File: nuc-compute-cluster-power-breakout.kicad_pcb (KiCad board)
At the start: 4 copper layers, 100 x 100 mm, 159 parts, among them J1 USB3106-30-0230-A, J10 10107844-002LF, J2 BM04B-SRSS-TB-LF-SN, J3 BM04B-SRSS-TB-LF-SN, J4 43045-1013, J5 430450812, J6 430450812, J7 430450812, J8 430450812, J9 430450812, Q1 SQS401EN-T1_BE3, Q10 SSM3K15ACT, Q11 BC856,215, Q15 DMN4010LFG-7, Q2 SQS401EN-T1_BE3, Q3 SSM3K15ACT, Q4 SSM3K15ACT, Q5 SQS401EN-T1_BE3, Q6 SSM3K15ACT, Q7 SQS401EN-T1_BE3, Q8 SQS401EN-T1_BE3, Q9 SSM3K15ACT, U1 FT2232HL-REEL, U10 TCA9534, U11 TMCS1100A2-Q1, U12 TMCS1100A2-Q1, U13 TMCS1100A2-Q1, U14 ADS7828, U15 AP62301WU-7, U7 AP62301WU-7, U8 TMCS1100A2-Q1, U9 TMCS1100A2-Q1, Y1 KX-7_12,MHz

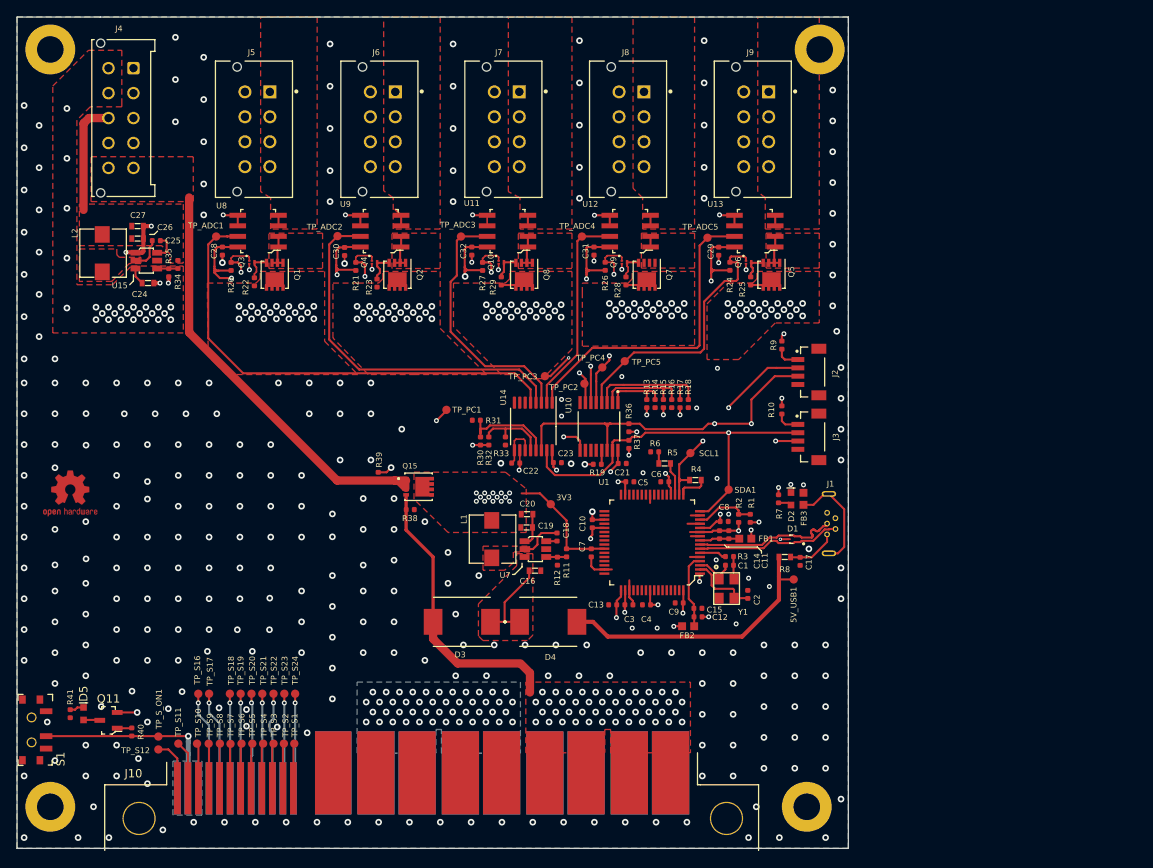
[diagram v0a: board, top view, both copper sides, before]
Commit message: Added board cut-out. Logos replacement
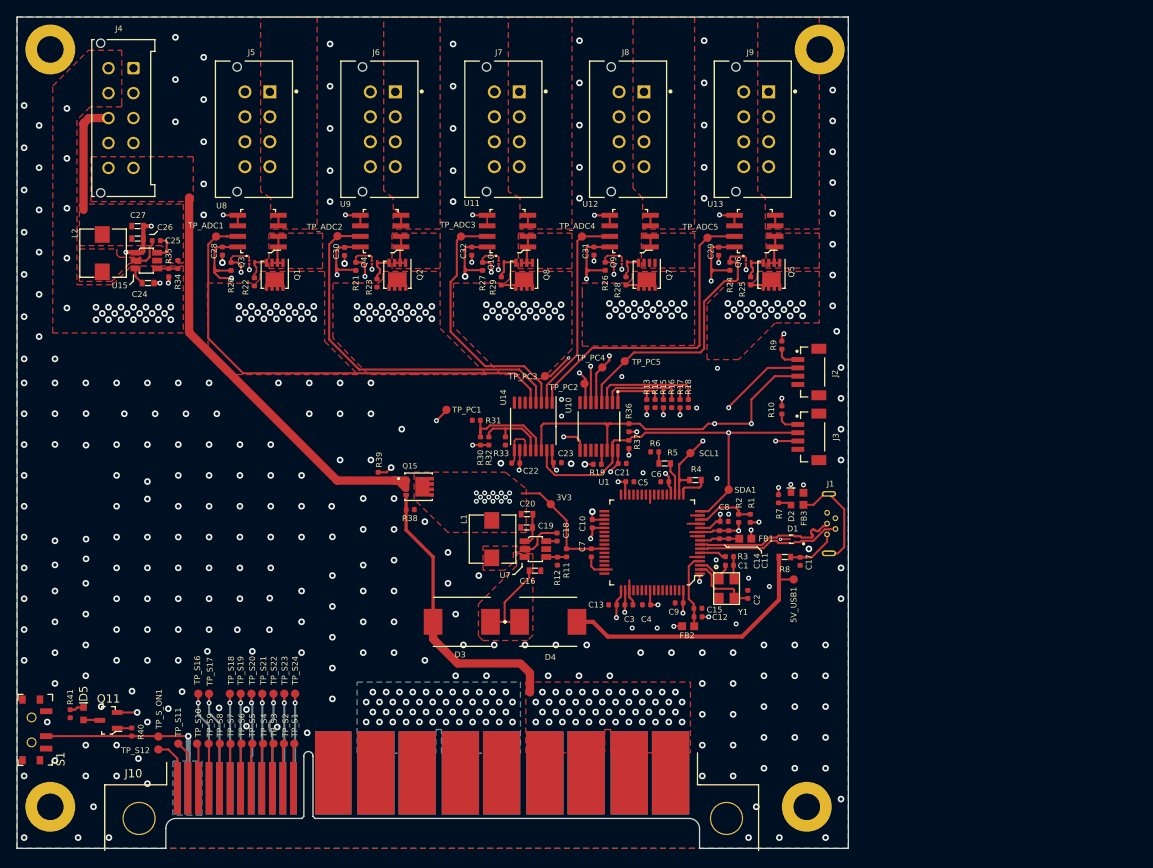
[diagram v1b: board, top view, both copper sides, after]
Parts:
- removed G***: antmicro-logo_scaled_20mm, antmicro-footprints:antmicro-logo_scaled_20mm_mask
- removed REF**: OSHW-Logo2_7.3x6mm_Copper_Mask, antmicro-footprints:OSHW-Logo2_7.3x6mm_Copper_Mask
- added N1: OSHW-Logo_7.5x8mm_Mask, antmicro-footprints:OSHW-Logo_7.5x8mm_Mask, F.Cu at (96.0, 107.8)
- added N2: antmicro-logo_scaled_20mm, antmicro-footprints:antmicro-logo_scaled_20mm_mask, F.Cu at (112.9, 107.1)
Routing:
- net VCC3V3: track 191.6 -> 189.5 mm
- net GND: vias 352 -> 333
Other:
- outline, holes or cut-outs redrawn

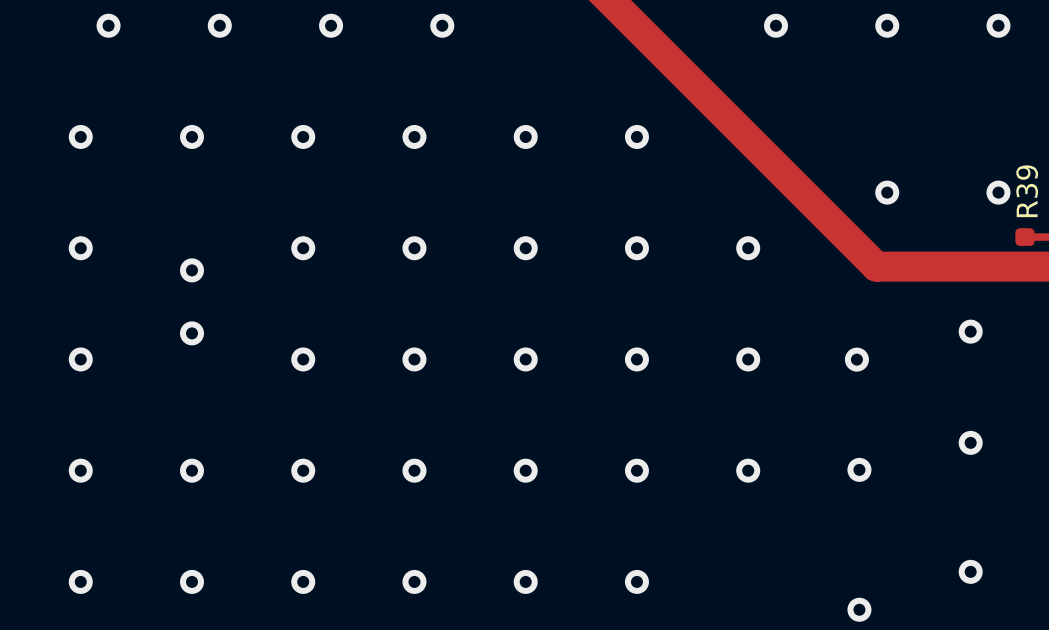
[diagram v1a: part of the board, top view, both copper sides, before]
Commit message: Change the board name
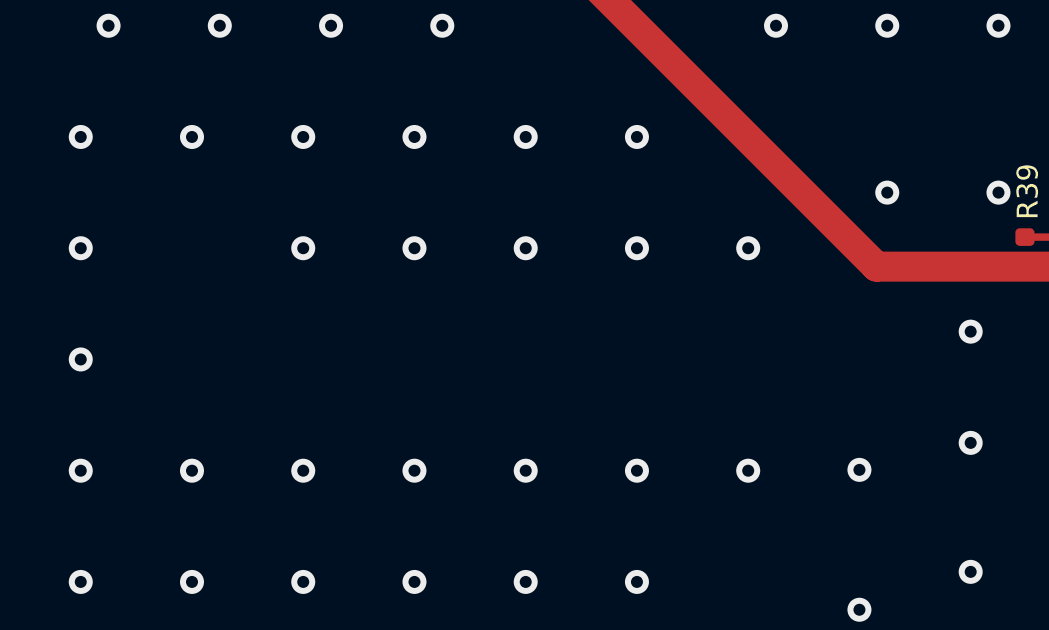
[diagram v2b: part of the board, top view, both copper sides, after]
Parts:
- moved N2 0.50 mm to (112.9, 107.6)
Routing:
- net GND: vias 333 -> 325
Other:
- board text added: "Server PSU Breakout Board"
- board text removed: "NUC Breakout Board"

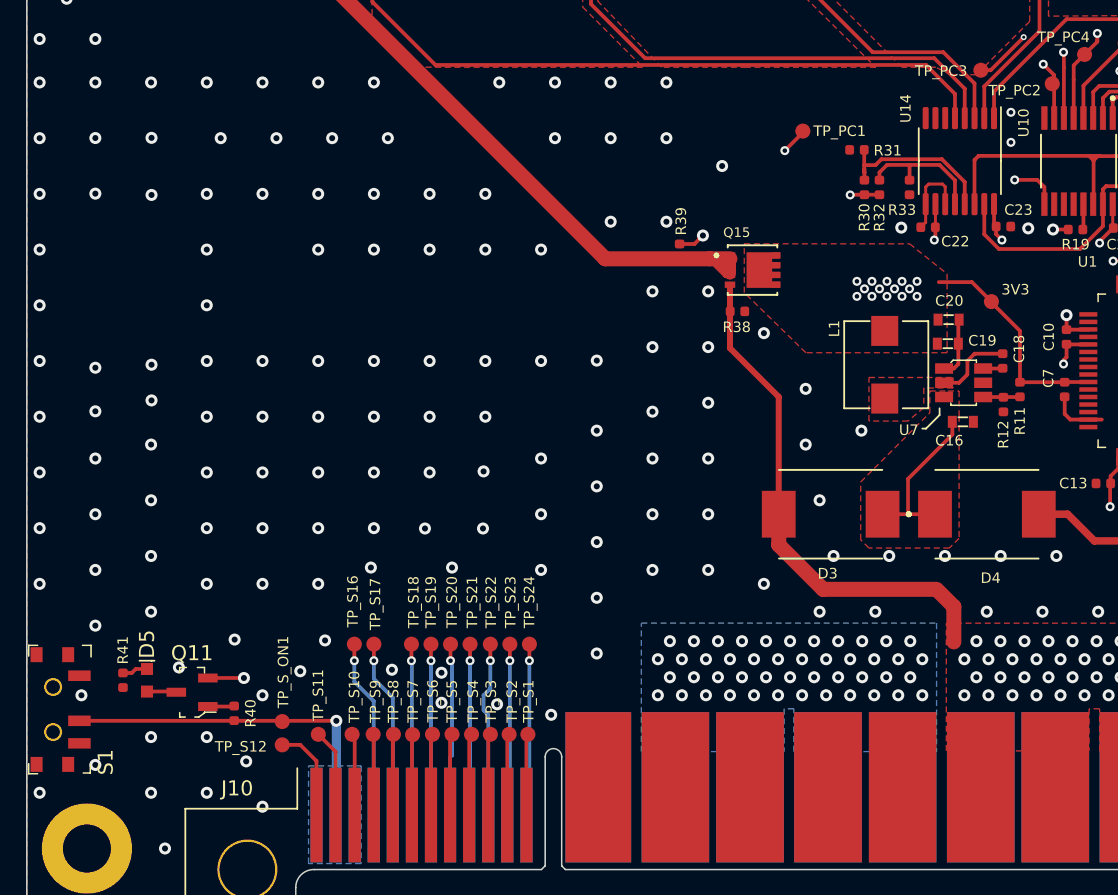
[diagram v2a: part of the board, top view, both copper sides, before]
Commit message: Unify the font
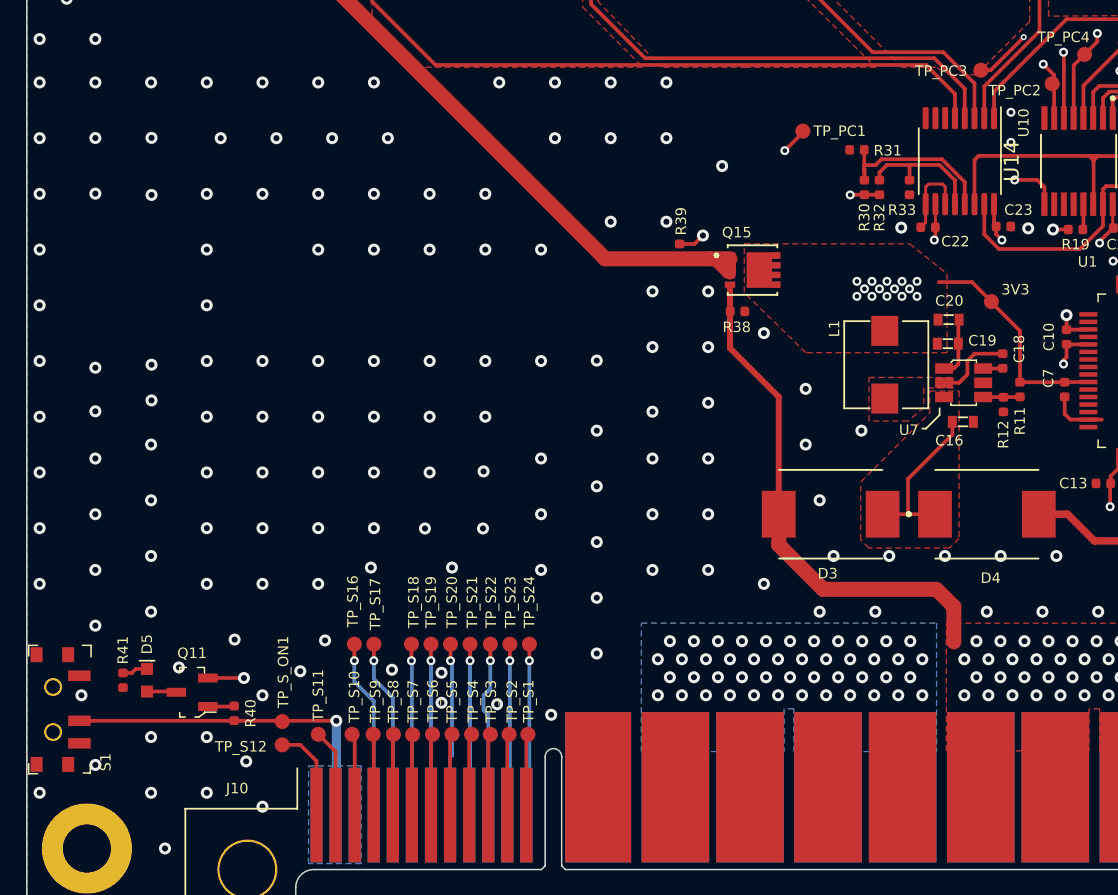
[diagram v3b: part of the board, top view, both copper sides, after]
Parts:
- N1: value OSHW-Logo_7.5x8mm_Mask -> oshw_logo
- N2: value antmicro-logo_scaled_20mm -> antmicro_logo
- U14: footprint nuc-compute-cluster-power-breakout-footprints:TSSOP-16_4.4x5mm_P0.65mm -> antmicro-footprints:TSSOP-16_4.4x5mm_P0.65mm
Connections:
- J1 pad 4: Net-(J1-Pad4) -> (no net)
- J10 pad P19/20: Net-(J10-PadP19/20) -> (no net)
- S1 pad 1: Net-(S1-Pad1) -> (no net)
- U1 pad 21: Net-(U1-Pad21) -> (no net)
- U1 pad 22: Net-(U1-Pad22) -> (no net)
- U1 pad 23: Net-(U1-Pad23) -> (no net)
- U1 pad 24: Net-(U1-Pad24) -> (no net)
- U1 pad 26: Net-(U1-Pad26) -> (no net)
- U1 pad 27: Net-(U1-Pad27) -> (no net)
- U1 pad 28: Net-(U1-Pad28) -> (no net)
- U1 pad 29: Net-(U1-Pad29) -> (no net)
- U1 pad 30: Net-(U1-Pad30) -> (no net)
- U1 pad 32: Net-(U1-Pad32) -> (no net)
- U1 pad 33: Net-(U1-Pad33) -> (no net)
- U1 pad 34: Net-(U1-Pad34) -> (no net)
- U1 pad 36: Net-(U1-Pad36) -> (no net)
- U1 pad 38: Net-(U1-Pad38) -> (no net)
- U1 pad 39: Net-(U1-Pad39) -> (no net)
- U1 pad 40: Net-(U1-Pad40) -> (no net)
- U1 pad 41: Net-(U1-Pad41) -> (no net)
- U1 pad 43: Net-(U1-Pad43) -> (no net)
- U1 pad 44: Net-(U1-Pad44) -> (no net)
- U1 pad 45: Net-(U1-Pad45) -> (no net)
- U1 pad 46: Net-(U1-Pad46) -> (no net)
- U1 pad 48: Net-(U1-Pad48) -> (no net)
- U1 pad 52: Net-(U1-Pad52) -> (no net)
- U1 pad 53: Net-(U1-Pad53) -> (no net)
- U1 pad 54: Net-(U1-Pad54) -> (no net)
- U1 pad 55: Net-(U1-Pad55) -> (no net)
- U1 pad 57: Net-(U1-Pad57) -> (no net)
- U1 pad 58: Net-(U1-Pad58) -> (no net)
- U1 pad 59: Net-(U1-Pad59) -> (no net)
- U1 pad 60: Net-(U1-Pad60) -> (no net)
- U1 pad 61: Net-(U1-Pad61) -> (no net)
- U1 pad 62: Net-(U1-Pad62) -> (no net)
- U1 pad 63: Net-(U1-Pad63) -> (no net)
- U10 pad 10: Net-(U10-Pad10) -> (no net)
- U10 pad 11: Net-(U10-Pad11) -> (no net)
- U10 pad 12: Net-(U10-Pad12) -> (no net)
- U14 pad 6: Net-(U14-Pad6) -> (no net)
- U14 pad 7: Net-(U14-Pad7) -> (no net)
- U14 pad 8: Net-(U14-Pad8) -> (no net)
- U15 pad 5: Net-(U15-Pad5) -> (no net)
- U7 pad 5: Net-(U7-Pad5) -> (no net)
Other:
- board text added: "Rev. 1.0.0"
- board text removed: "Rev. 1.0"
